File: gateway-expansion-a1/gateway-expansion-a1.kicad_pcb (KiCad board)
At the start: 2 copper layers, 107 x 86 mm, 3 parts, among them J1 Ruuvi Connector, J2 Ruuvi Connector, J3 Ruuvi Connector

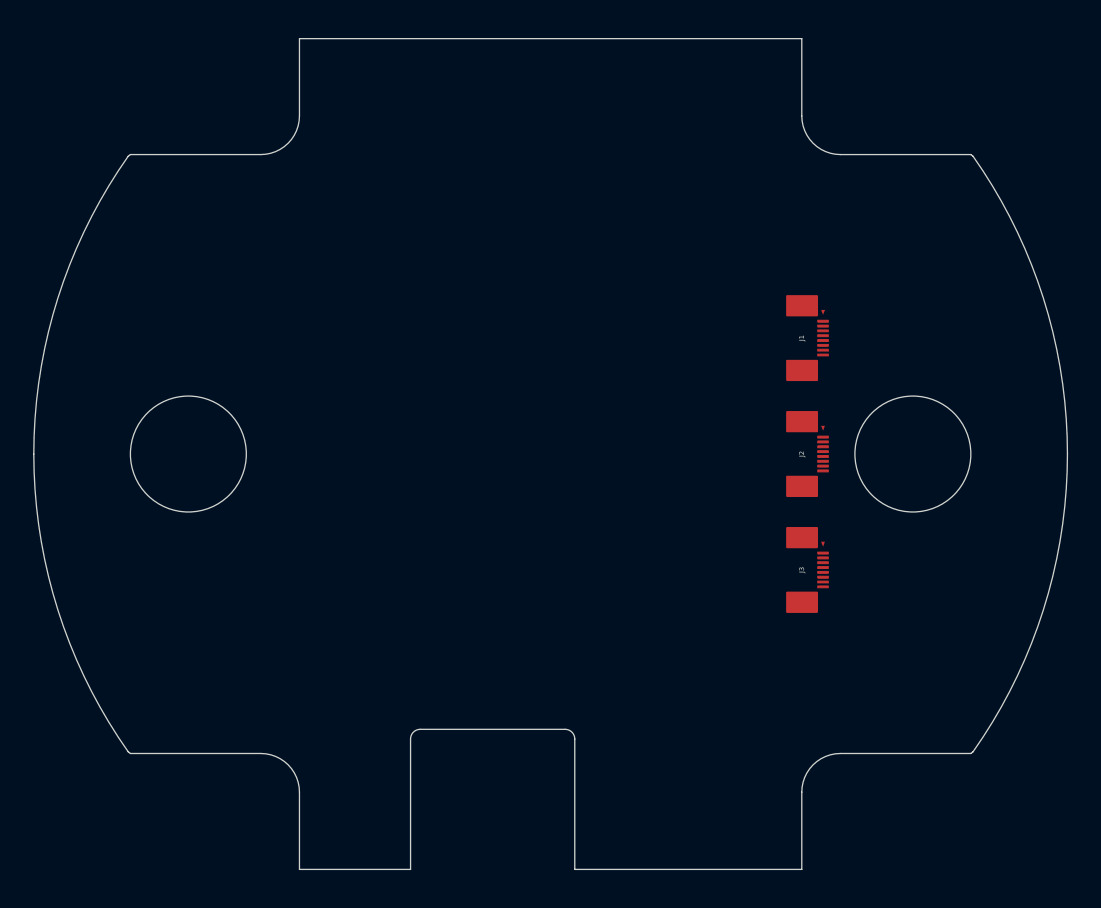
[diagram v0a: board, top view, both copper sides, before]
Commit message: Add copper zones and export gerbers
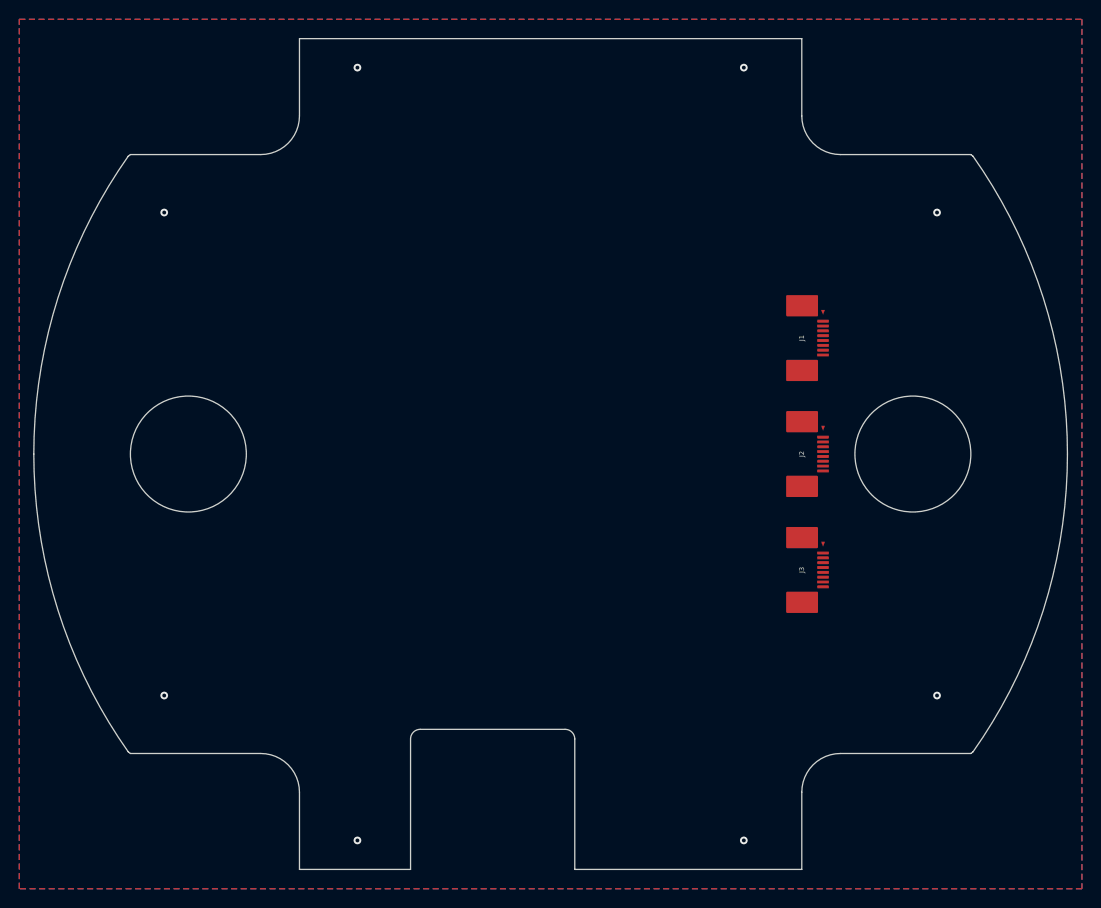
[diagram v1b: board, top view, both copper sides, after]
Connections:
- J1 pad 8: Net-(J1-Pad8) -> GND
- J2 pad 8: Net-(J2-Pad8) -> GND
- J3 pad 8: Net-(J3-Pad8) -> GND
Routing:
- net GND: vias 0 -> 8
- added copper zone on B.Cu, net GND
- added copper zone on F.Cu, net GND
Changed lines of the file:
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@@
     (thickness 1.6)
     (drawings 60)
-    (tracks 0)
+    (tracks 8)
     (modules 3)
-    (nets 25)
+    (nets 23)
   )
   (paper "A4")
@@
     )
     (pcbplotparams
-      (layerselection 0x01000_7ffffffe)
-      (usegerberextensions false)
+      (layerselection 0x010c0_ffffffff)
+      (usegerberextensions true)
       (usegerberattributes true)
       (usegerberadvancedattributes true)
@@
       (sketchpadsonfab false)
       (subtractmaskfromsilk false)
-      (outputformat 3)
+      (outputformat 1)
       (mirror false)
       (drillshape 0)
@@
   )
   (net 0 "")
-  (net 1 "Net-(J1-Pad8)")
+  (net 1 "GND")
   (net 2 "Net-(J1-Pad7)")
   (net 3 "Net-(J1-Pad6)")
@@
   (net 7 "Net-(J1-Pad2)")
   (net 8 "Net-(J1-Pad1)")
-  (net 9 "Net-(J2-Pad8)")
-  (net 10 "Net-(J2-Pad7)")
-  (net 11 "Net-(J2-Pad6)")
-  (net 12 "Net-(J2-Pad5)")
-  (net 13 "Net-(J2-Pad4)")
-  (net 14 "Net-(J2-Pad3)")
-  (net 15 "Net-(J2-Pad2)")
-  (net 16 "Net-(J2-Pad1)")
-  (net 17 "Net-(J3-Pad8)")
-  (net 18 "Net-(J3-Pad7)")
-  (net 19 "Net-(J3-Pad6)")
-  (net 20 "Net-(J3-Pad5)")
-  (net 21 "Net-(J3-Pad4)")
-  (net 22 "Net-(J3-Pad3)")
-  (net 23 "Net-(J3-Pad2)")
-  (net 24 "Net-(J3-Pad1)")
+  (net 9 "Net-(J2-Pad7)")
+  (net 10 "Net-(J2-Pad6)")
+  (net 11 "Net-(J2-Pad5)")
+  (net 12 "Net-(J2-Pad4)")
+  (net 13 "Net-(J2-Pad3)")
+  (net 14 "Net-(J2-Pad2)")
+  (net 15 "Net-(J2-Pad1)")
+  (net 16 "Net-(J3-Pad7)")
+  (net 17 "Net-(J3-Pad6)")
+  (net 18 "Net-(J3-Pad5)")
+  (net 19 "Net-(J3-Pad4)")
+  (net 20 "Net-(J3-Pad3)")
+  (net 21 "Net-(J3-Pad2)")
+  (net 22 "Net-(J3-Pad1)")
   (module "connector:RUUVI_CONNECTOR_FFC" (layer "F.Cu")
     (at 176 88 -90)
@@
       (net 2 "Net-(J1-Pad7)") (pinfunction "Pin_7"))
     (pad "8" smd roundrect (at 1.75 -2.2 270) (size 0.3 1.2) (layers "F.Cu" "F.Paste" "F.Mask") (roundrect_rratio 0.167)
-      (net 1 "Net-(J1-Pad8)") (pinfunction "Pin_8"))
+      (net 1 "GND") (pinfunction "Pin_8"))
     (pad "~" smd roundrect (at 3.35 -0.03 270) (size 2.2 3.3) (layers "F.Cu" "F.Paste" "F.Mask") (roundrect_rratio 0.045))
     (pad "~" smd trapezoid (at -2.67 -2.2 270) (size 0.5 0.2) (rect_delta 0.19 0 ) (layers "F.Cu" "F.Mask"))
@@
     (fp_line (start 4.8 3.6) (end 4.8 3) (layer "F.CrtYd") (width 0.05))
     (pad "1" smd roundrect (at -1.75 -2.2 270) (size 0.3 1.2) (layers "F.Cu" "F.Paste" "F.Mask") (roundrect_rratio 0.167)
-      (net 24 "Net-(J3-Pad1)") (pinfunction "Pin_1"))
+      (net 22 "Net-(J3-Pad1)") (pinfunction "Pin_1"))
     (pad "2" smd roundrect (at -1.25 -2.2 270) (size 0.3 1.2) (layers "F.Cu" "F.Paste" "F.Mask") (roundrect_rratio 0.167)
-      (net 23 "Net-(J3-Pad2)") (pinfunction "Pin_2"))
+      (net 21 "Net-(J3-Pad2)") (pinfunction "Pin_2"))
     (pad "3" smd roundrect (at -0.75 -2.2 270) (size 0.3 1.2) (layers "F.Cu" "F.Paste" "F.Mask") (roundrect_rratio 0.167)
-      (net 22 "Net-(J3-Pad3)") (pinfunction "Pin_3"))
+      (net 20 "Net-(J3-Pad3)") (pinfunction "Pin_3"))
     (pad "4" smd roundrect (at -0.25 -2.2 270) (size 0.3 1.2) (layers "F.Cu" "F.Paste" "F.Mask") (roundrect_rratio 0.167)
-      (net 21 "Net-(J3-Pad4)") (pinfunction "Pin_4"))
+      (net 19 "Net-(J3-Pad4)") (pinfunction "Pin_4"))
     (pad "5" smd roundrect (at 0.25 -2.2 270) (size 0.3 1.2) (layers "F.Cu" "F.Paste" "F.Mask") (roundrect_rratio 0.167)
-      (net 20 "Net-(J3-Pad5)") (pinfunction "Pin_5"))
+      (net 18 "Net-(J3-Pad5)") (pinfunction "Pin_5"))
     (pad "6" smd roundrect (at 0.75 -2.2 270) (size 0.3 1.2) (layers "F.Cu" "F.Paste" "F.Mask") (roundrect_rratio 0.167)
-      (net 19 "Net-(J3-Pad6)") (pinfunction "Pin_6"))
+      (net 17 "Net-(J3-Pad6)") (pinfunction "Pin_6"))
     (pad "7" smd roundrect (at 1.25 -2.2 270) (size 0.3 1.2) (layers "F.Cu" "F.Paste" "F.Mask") (roundrect_rratio 0.167)
-      (net 18 "Net-(J3-Pad7)") (pinfunction "Pin_7"))
+      (net 16 "Net-(J3-Pad7)") (pinfunction "Pin_7"))
     (pad "8" smd roundrect (at 1.75 -2.2 270) (size 0.3 1.2) (layers "F.Cu" "F.Paste" "F.Mask") (roundrect_rratio 0.167)
-      (net 17 "Net-(J3-Pad8)") (pinfunction "Pin_8"))
+      (net 1 "GND") (pinfunction "Pin_8"))
     (pad "~" smd roundrect (at -3.35 -0.03 270) (size 2.2 3.3) (layers "F.Cu" "F.Paste" "F.Mask") (roundrect_rratio 0.045))
     (pad "~" smd trapezoid (at -2.67 -2.2 270) (size 0.5 0.2) (rect_delta 0.19 0 ) (layers "F.Cu" "F.Mask"))
@@
     (fp_line (start 4.8 3.6) (end 4.8 3) (layer "F.CrtYd") (width 0.05))
     (pad "1" smd roundrect (at -1.75 -2.2 270) (size 0.3 1.2) (layers "F.Cu" "F.Paste" "F.Mask") (roundrect_rratio 0.167)
-      (net 16 "Net-(J2-Pad1)") (pinfunction "Pin_1"))
+      (net 15 "Net-(J2-Pad1)") (pinfunction "Pin_1"))
     (pad "2" smd roundrect (at -1.25 -2.2 270) (size 0.3 1.2) (layers "F.Cu" "F.Paste" "F.Mask") (roundrect_rratio 0.167)
-      (net 15 "Net-(J2-Pad2)") (pinfunction "Pin_2"))
+      (net 14 "Net-(J2-Pad2)") (pinfunction "Pin_2"))
     (pad "3" smd roundrect (at -0.75 -2.2 270) (size 0.3 1.2) (layers "F.Cu" "F.Paste" "F.Mask") (roundrect_rratio 0.167)
-      (net 14 "Net-(J2-Pad3)") (pinfunction "Pin_3"))
+      (net 13 "Net-(J2-Pad3)") (pinfunction "Pin_3"))
     (pad "4" smd roundrect (at -0.25 -2.2 270) (size 0.3 1.2) (layers "F.Cu" "F.Paste" "F.Mask") (roundrect_rratio 0.167)
-      (net 13 "Net-(J2-Pad4)") (pinfunction "Pin_4"))
+      (net 12 "Net-(J2-Pad4)") (pinfunction "Pin_4"))
     (pad "5" smd roundrect (at 0.25 -2.2 270) (size 0.3 1.2) (layers "F.Cu" "F.Paste" "F.Mask") (roundrect_rratio 0.167)
-      (net 12 "Net-(J2-Pad5)") (pinfunction "Pin_5"))
+      (net 11 "Net-(J2-Pad5)") (pinfunction "Pin_5"))
     (pad "6" smd roundrect (at 0.75 -2.2 270) (size 0.3 1.2) (layers "F.Cu" "F.Paste" "F.Mask") (roundrect_rratio 0.167)
-      (net 11 "Net-(J2-Pad6)") (pinfunction "Pin_6"))
+      (net 10 "Net-(J2-Pad6)") (pinfunction "Pin_6"))
     (pad "7" smd roundrect (at 1.25 -2.2 270) (size 0.3 1.2) (layers "F.Cu" "F.Paste" "F.Mask") (roundrect_rratio 0.167)
-      (net 10 "Net-(J2-Pad7)") (pinfunction "Pin_7"))
+      (net 9 "Net-(J2-Pad7)") (pinfunction "Pin_7"))
     (pad "8" smd roundrect (at 1.75 -2.2 270) (size 0.3 1.2) (layers "F.Cu" "F.Paste" "F.Mask") (roundrect_rratio 0.167)
-      (net 9 "Net-(J2-Pad8)") (pinfunction "Pin_8"))
+      (net 1 "GND") (pinfunction "Pin_8"))
     (pad "~" smd roundrect (at 3.35 -0.03 270) (size 2.2 3.3) (layers "F.Cu" "F.Paste" "F.Mask") (roundrect_rratio 0.045))
     (pad "~" smd trapezoid (at -2.67 -2.2 270) (size 0.5 0.2) (rect_delta 0.19 0 ) (layers "F.Cu" "F.Mask"))
@@
     (effects (font (size 1.5 1.5) (thickness 0.1) italic))
   )
+  (via (at 130 140) (size 0.8) (drill 0.4) (layers "F.Cu" "B.Cu") (net 1))
+  (via (at 190 125) (size 0.8) (drill 0.4) (layers "F.Cu" "B.Cu") (net 1))
+  (via (at 190 75) (size 0.8) (drill 0.4) (layers "F.Cu" "B.Cu") (net 1))
+  (via (at 170 60) (size 0.8) (drill 0.4) (layers "F.Cu" "B.Cu") (net 1))
+  (via (at 110 75) (size 0.8) (drill 0.4) (layers "F.Cu" "B.Cu") (net 1))
+  (via (at 170 140) (size 0.8) (drill 0.4) (layers "F.Cu" "B.Cu") (net 1))
+  (via (at 110 125) (size 0.8) (drill 0.4) (layers "F.Cu" "B.Cu") (net 1))
+  (via (at 130 60) (size 0.8) (drill 0.4) (layers "F.Cu" "B.Cu") (net 1))
+  (zone (net 1) (net_name "GND") (layers F&B.Cu) (hatch edge 0.508)
+    (connect_pads (clearance 0.2))
+    (min_thickness 0.2)
+    (fill yes (thermal_gap 0.2) (thermal_bridge_width 0.25))
+    (polygon
+      (pts
+        (xy 205 145) (xy 95 145) (xy 95 55) (xy 205 55)
+      )
+    )
+  )
 )

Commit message: Update outlines
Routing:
- net GND: vias 8 -> 4
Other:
- board size 107 x 86 mm -> 107 x 77 mm
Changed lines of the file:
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@@
   (general
     (thickness 1.6)
-    (drawings 60)
-    (tracks 8)
+    (drawings 68)
+    (tracks 4)
     (modules 3)
     (nets 23)
@@
   (gr_line (start 137.6 137.2) (end 150.4 137.2) (layer "Dwgs.User") (width 0.1))
   (gr_line (start 180 67.300001) (end 180 132.7) (layer "Dwgs.User") (width 0.1))
-  (gr_arc (start 150 100) (end 203.5 100) (angle -35.17639349) (layer "Edge.Cuts") (width 0.1))
-  (gr_line (start 152.5 143) (end 176 143) (layer "Edge.Cuts") (width 0.1))
-  (gr_line (start 120.000001 131.000001) (end 106.5 131) (layer "Edge.Cuts") (width 0.1))
-  (gr_arc (start 150 100) (end 203.5 100) (angle 35.17639349) (layer "Edge.Cuts") (width 0.1))
+  (gr_line (start 108.7 134) (end 108.606652 133.894553) (layer "Edge.Cuts") (width 0.1))
+  (gr_line (start 135.5 131) (end 120 131) (layer "Edge.Cuts") (width 0.1))
   (gr_arc (start 151.5 129.5) (end 151.5 128.5) (angle 90) (layer "Edge.Cuts") (width 0.1))
-  (gr_line (start 152.5 129.5) (end 152.5 143) (layer "Edge.Cuts") (width 0.1))
-  (gr_line (start 176 135) (end 176 143) (layer "Edge.Cuts") (width 0.1))
-  (gr_line (start 193.729954 69.178886) (end 193.500001 68.999999) (layer "Edge.Cuts") (width 0.1))
+  (gr_line (start 179.000003 61.100002) (end 179.000002 57) (layer "Edge.Cuts") (width 0.1))
+  (gr_line (start 152.5 129.5) (end 152.5 131) (layer "Edge.Cuts") (width 0.1))
+  (gr_line (start 183.900001 66.000001) (end 183.849798 66.08584) (layer "Edge.Cuts") (width 0.1))
+  (gr_line (start 116.1 134) (end 108.7 134) (layer "Edge.Cuts") (width 0.1))
+  (gr_line (start 108.700001 65.999999) (end 108.606652 66.105447) (layer "Edge.Cuts") (width 0.1))
+  (gr_line (start 179.000003 61.100002) (end 178.91416 61.1502) (layer "Edge.Cuts") (width 0.1))
+  (gr_line (start 116.100002 66.000001) (end 116.150201 66.08584) (layer "Edge.Cuts") (width 0.1))
+  (gr_arc (start 120 135) (end 120 131) (angle -74.24882634) (layer "Edge.Cuts") (width 0.1))
   (gr_circle (center 187.5 100) (end 193.5 100) (layer "Edge.Cuts") (width 0.1))
-  (gr_arc (start 120 134.999998) (end 120.000001 131.000001) (angle 90) (layer "Edge.Cuts") (width 0.1))
-  (gr_line (start 124 57) (end 176 57) (layer "Edge.Cuts") (width 0.1))
-  (gr_line (start 135.5 143) (end 135.5 129.5) (layer "Edge.Cuts") (width 0.1))
-  (gr_line (start 124 65) (end 124 57) (layer "Edge.Cuts") (width 0.1))
+  (gr_line (start 183.9 134) (end 191.3 134) (layer "Edge.Cuts") (width 0.1))
+  (gr_line (start 121 57) (end 179.000002 57) (layer "Edge.Cuts") (width 0.1))
+  (gr_line (start 135.5 131) (end 135.5 129.5) (layer "Edge.Cuts") (width 0.1))
+  (gr_line (start 121 61.1) (end 121 57) (layer "Edge.Cuts") (width 0.1))
+  (gr_arc (start 180 65) (end 176 65) (angle 74.24882634) (layer "Edge.Cuts") (width 0.1))
   (gr_line (start 136.5 128.5) (end 151.5 128.5) (layer "Edge.Cuts") (width 0.1))
-  (gr_line (start 179.999999 131.000001) (end 193.5 131) (layer "Edge.Cuts") (width 0.1))
-  (gr_line (start 180 69) (end 193.500001 68.999999) (layer "Edge.Cuts") (width 0.1))
-  (gr_arc (start 150 100) (end 96.5 100) (angle -35.17639349) (layer "Edge.Cuts") (width 0.1))
-  (gr_line (start 106.270045 69.178887) (end 106.5 69) (layer "Edge.Cuts") (width 0.1))
+  (gr_line (start 152.5 131) (end 180 131) (layer "Edge.Cuts") (width 0.1))
+  (gr_arc (start 180 65) (end 180 69) (angle -74.24882634) (layer "Edge.Cuts") (width 0.1))
+  (gr_arc (start 150 100) (end 96.5 100) (angle -39.31200875) (layer "Edge.Cuts") (width 0.1))
+  (gr_line (start 183.9 134) (end 183.849799 133.914159) (layer "Edge.Cuts") (width 0.1))
+  (gr_arc (start 180 65) (end 180 69) (angle 90) (layer "Edge.Cuts") (width 0.1))
+  (gr_line (start 121 61.1) (end 121.085841 61.150201) (layer "Edge.Cuts") (width 0.1))
   (gr_arc (start 120 65) (end 120 69) (angle -90) (layer "Edge.Cuts") (width 0.1))
-  (gr_line (start 193.729954 130.821114) (end 193.5 131) (layer "Edge.Cuts") (width 0.1))
+  (gr_arc (start 150 100) (end 203.5 100) (angle 39.31200875) (layer "Edge.Cuts") (width 0.1))
+  (gr_line (start 116.100002 66.000001) (end 108.700001 65.999999) (layer "Edge.Cuts") (width 0.1))
+  (gr_line (start 191.299999 65.999999) (end 191.393349 66.105448) (layer "Edge.Cuts") (width 0.1))
   (gr_circle (center 112.5 100) (end 118.5 100) (layer "Edge.Cuts") (width 0.1))
-  (gr_line (start 124 135) (end 124 143) (layer "Edge.Cuts") (width 0.1))
-  (gr_line (start 176 65) (end 176 57) (layer "Edge.Cuts") (width 0.1))
-  (gr_arc (start 150 100) (end 96.5 100) (angle 35.17639152) (layer "Edge.Cuts") (width 0.1))
-  (gr_line (start 120 69) (end 106.5 69) (layer "Edge.Cuts") (width 0.1))
-  (gr_line (start 135.5 143) (end 124 143) (layer "Edge.Cuts") (width 0.1))
+  (gr_line (start 183.900001 66.000001) (end 191.299999 65.999999) (layer "Edge.Cuts") (width 0.1))
   (gr_arc (start 136.5 129.5) (end 135.5 129.5) (angle 90) (layer "Edge.Cuts") (width 0.1))
-  (gr_arc (start 180 134.999998) (end 179.999999 131.000001) (angle -90) (layer "Edge.Cuts") (width 0.1))
-  (gr_line (start 106.270046 130.821114) (end 106.5 131) (layer "Edge.Cuts") (width 0.1))
-  (gr_arc (start 180.000001 65.000001) (end 180 69) (angle 90) (layer "Edge.Cuts") (width 0.1))
+  (gr_line (start 191.3 134) (end 191.393348 133.894553) (layer "Edge.Cuts") (width 0.1))
+  (gr_line (start 116.1 134) (end 116.150201 133.914159) (layer "Edge.Cuts") (width 0.1))
+  (gr_arc (start 150 99.999999) (end 203.499998 100) (angle -39.31200875) (layer "Edge.Cuts") (width 0.1))
+  (gr_arc (start 180 135) (end 180 131) (angle 74.24882634) (layer "Edge.Cuts") (width 0.1))
+  (gr_arc (start 120 65) (end 120 69) (angle 74.24882634) (layer "Edge.Cuts") (width 0.1))
+  (gr_arc (start 120 65) (end 124 65) (angle -74.24882634) (layer "Edge.Cuts") (width 0.1))
+  (gr_arc (start 149.999998 100) (end 96.499999 99.999999) (angle 39.31200875) (layer "Edge.Cuts") (width 0.1))
   (gr_text "Room for sensors and antennas" (at 103 100 90) (layer "Dwgs.User")
     (effects (font (size 1.5 1.5) (thickness 0.1) italic))
@@
     (effects (font (size 1.5 1.5) (thickness 0.1) italic))
   )
-  (via (at 130 140) (size 0.8) (drill 0.4) (layers "F.Cu" "B.Cu") (net 1))
   (via (at 190 125) (size 0.8) (drill 0.4) (layers "F.Cu" "B.Cu") (net 1))
   (via (at 190 75) (size 0.8) (drill 0.4) (layers "F.Cu" "B.Cu") (net 1))
-  (via (at 170 60) (size 0.8) (drill 0.4) (layers "F.Cu" "B.Cu") (net 1))
   (via (at 110 75) (size 0.8) (drill 0.4) (layers "F.Cu" "B.Cu") (net 1))
-  (via (at 170 140) (size 0.8) (drill 0.4) (layers "F.Cu" "B.Cu") (net 1))
   (via (at 110 125) (size 0.8) (drill 0.4) (layers "F.Cu" "B.Cu") (net 1))
-  (via (at 130 60) (size 0.8) (drill 0.4) (layers "F.Cu" "B.Cu") (net 1))
   (zone (net 1) (net_name "GND") (layers F&B.Cu) (hatch edge 0.508)
     (connect_pads (clearance 0.2))
